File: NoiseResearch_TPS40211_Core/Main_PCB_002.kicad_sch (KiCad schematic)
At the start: 42 parts, among them IC1 TPS40211QDGQRQ1, Q1 AON7407, U12 MCP9700AT-ETT, U13 MCP9700AT-ETT, U2 Mounting_Hole_M2, U3 Mounting_Hole_M2, U4 Mounting_Hole_M2, U5 Mounting_Hole_M2

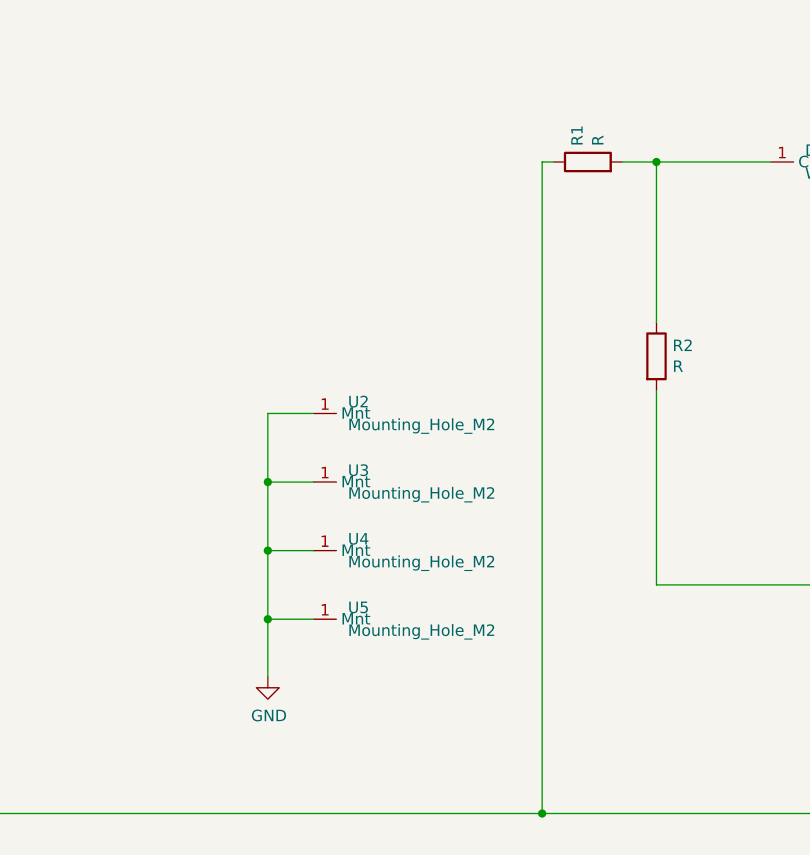
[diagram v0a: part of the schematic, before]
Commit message: Noise research for TSP40211 004
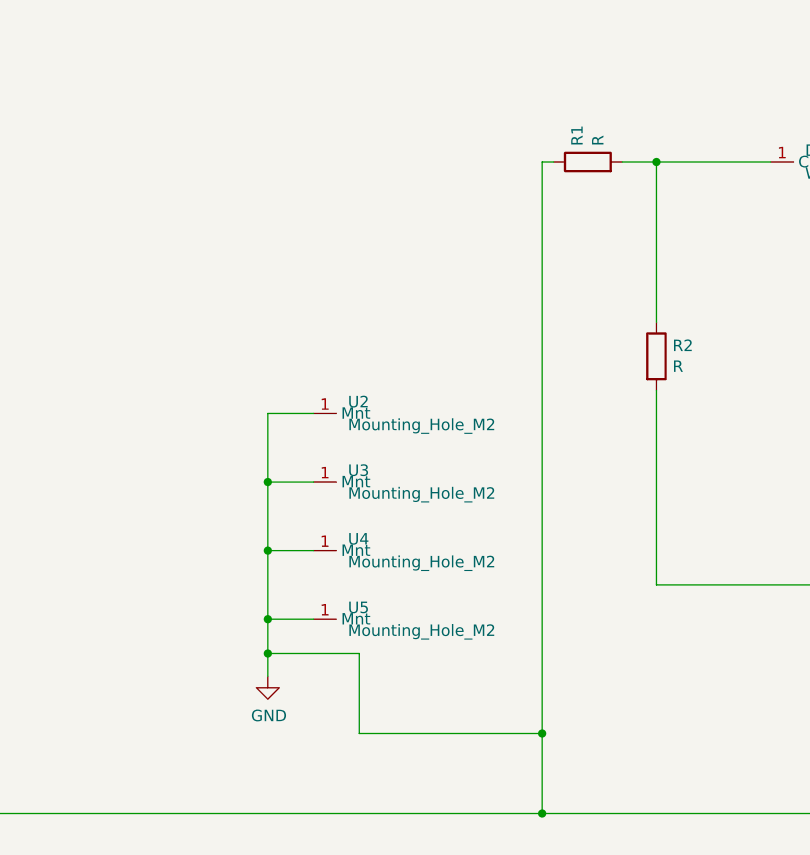
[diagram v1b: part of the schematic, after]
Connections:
- net GND: now also C11.2, C12.2, C13.2, C3.1, C30.2, C4.1, C49.2, C5.2, C50.2, C8.2, C9.2, D1.1 (Conn), D69.1 (Conn), IC1.11 (EP), IC1.6 (GND), R1.1, R8.2, U12.3 (GND), U13.3 (GND)
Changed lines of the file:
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@@
   (junction (at 335.28 133.35) (diameter 0) (color 0 0 0 0)
   )
+  (junction (at 129.54 229.87) (diameter 0) (color 0 0 0 0)
+  )
+  (junction (at 160.02 238.76) (diameter 0) (color 0 0 0 0)
+  )
   (junction (at 327.66 133.35) (diameter 0) (color 0 0 0 0)
   )
@@
     (stroke (width 0) (type default))
   )
+  (wire (pts (xy 129.54 229.87) (xy 139.7 229.87))
+    (stroke (width 0) (type default))
+  )
   (wire (pts (xy 349.25 133.35) (xy 351.79 133.35))
     (stroke (width 0) (type default))
@@
     (stroke (width 0) (type default))
   )
-  (wire (pts (xy 129.54 226.06) (xy 129.54 232.41))
+  (wire (pts (xy 129.54 226.06) (xy 129.54 229.87))
     (stroke (width 0) (type default))
   )
@@
     (stroke (width 0) (type default))
   )
-  (wire (pts (xy 160.02 175.26) (xy 160.02 247.65))
+  (wire (pts (xy 160.02 175.26) (xy 160.02 238.76))
     (stroke (width 0) (type default))
   )
@@
     (stroke (width 0) (type default))
   )
+  (wire (pts (xy 139.7 229.87) (xy 139.7 238.76))
+    (stroke (width 0) (type default))
+  )
   (wire (pts (xy 234.95 234.95) (xy 234.95 218.44))
     (stroke (width 0) (type default))
@@
     (stroke (width 0) (type default))
   )
+  (wire (pts (xy 129.54 229.87) (xy 129.54 232.41))
+    (stroke (width 0) (type default))
+  )
   (wire (pts (xy 325.12 133.35) (xy 327.66 133.35))
     (stroke (width 0) (type default))
   )
+  (wire (pts (xy 139.7 238.76) (xy 160.02 238.76))
+    (stroke (width 0) (type default))
+  )
   (wire (pts (xy 161.29 175.26) (xy 160.02 175.26))
     (stroke (width 0) (type default))
@@
     (stroke (width 0) (type default))
   )
+  (wire (pts (xy 160.02 238.76) (xy 160.02 247.65))
+    (stroke (width 0) (type default))
+  )
